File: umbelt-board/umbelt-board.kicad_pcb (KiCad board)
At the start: 4 copper layers, 56.6 x 20.3 mm, 101 parts, among them J1 USB4105-GF-A, J2 Conn_01x06, J3 SM04B-SRSS-TB, J4 TC2050-IDC-NL, J5 BM02B-ACHLKS, J6 Conn_Flex_Motor, J7 Conn_Indiv_Motor, Q1 AO3415A, SW1 KMR231NG-ULC-LFS, SW2 CUS-12TB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

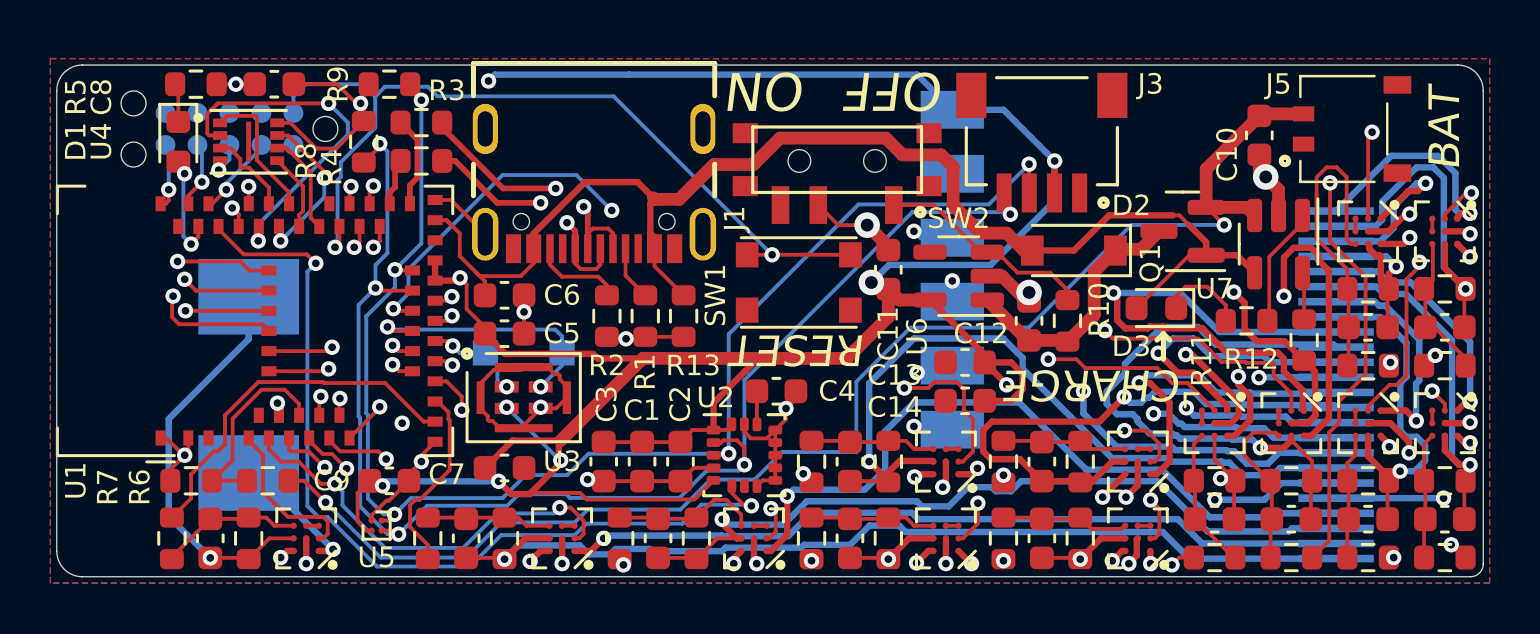
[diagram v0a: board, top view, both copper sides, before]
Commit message: complete routing. passes important DRC checks
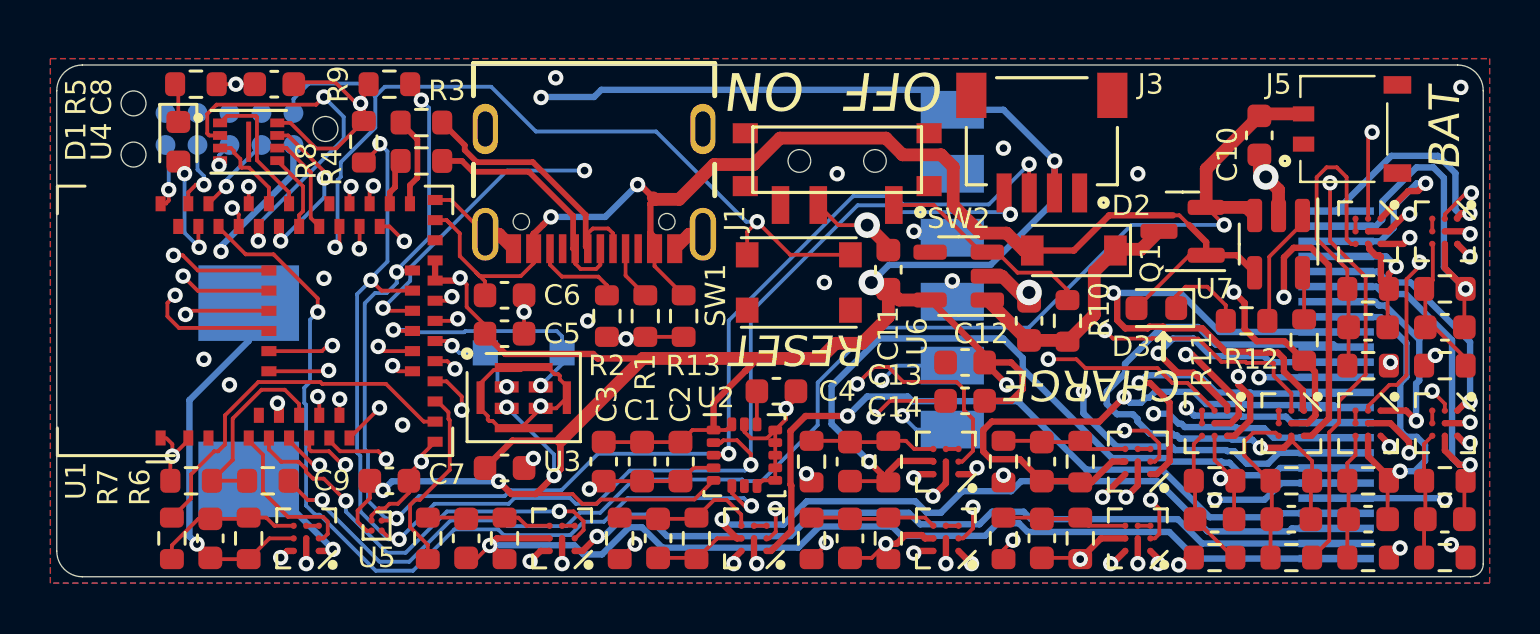
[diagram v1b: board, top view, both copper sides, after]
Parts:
- moved J7 0.25 mm to (134.6, 119.6)
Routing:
- net +3V3: track 239.8 -> 259.8 mm, vias 23 -> 25
- net GND: track 77.8 -> 84.3 mm, vias 26 -> 37
- net /SCL: track 55.0 -> 57.7 mm
- net /motor_drivers/OUT+_1: track 38.2 -> 40.3 mm
- net /motor_drivers/OUT+_4: track 30.3 -> 32.3 mm
- net /MOTOR_PWM_10: track 56.9 -> 58.7 mm
- net /MOTOR_PWM_3: track 31.1 -> 32.5 mm
- net /MOTOR_PWM_2: track 20.3 -> 21.7 mm
- net /SDA: track 55.7 -> 57.0 mm
- net /MOTOR_PWM_7: track 58.4 -> 59.6 mm
- net /MOTOR_PWM_5: track 37.8 -> 38.9 mm
- net /motor_drivers/OUT-_1: track 31.4 -> 32.5 mm
- net /MOTOR_EN_6: track 48.4 -> 49.5 mm
- net /A0: track 35.7 -> 36.7 mm
- net /motor_drivers/OUT-_2: track 28.8 -> 29.6 mm
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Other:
- board text added: "License: CERN-OHL-W v2+ github.com/cygann/umbelt-hw"

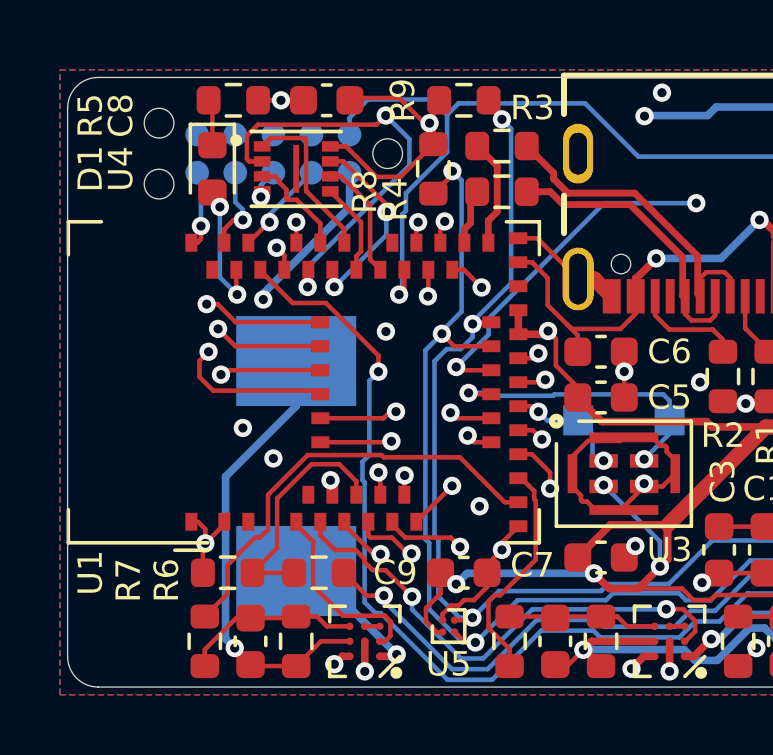
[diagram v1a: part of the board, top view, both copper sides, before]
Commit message: tweak ground pours
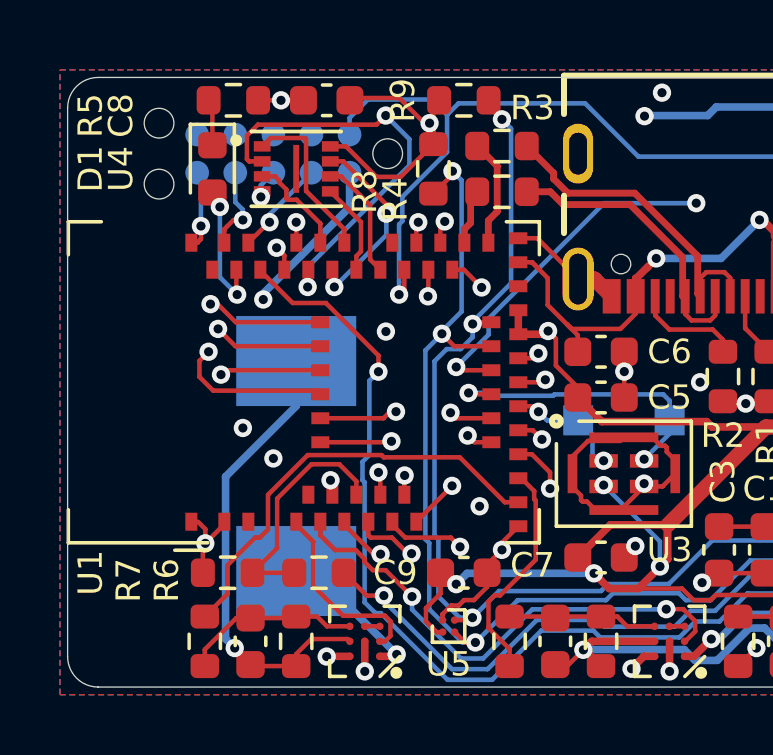
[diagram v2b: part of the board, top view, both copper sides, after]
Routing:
- net /D0: track 34.2 -> 32.0 mm
- net /MOTOR_EN_6: track 49.5 -> 48.9 mm

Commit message: complete flex pcb, generate gerbers for both boards
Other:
- rule pad_to_mask_clearance: 0.0508 -> 0

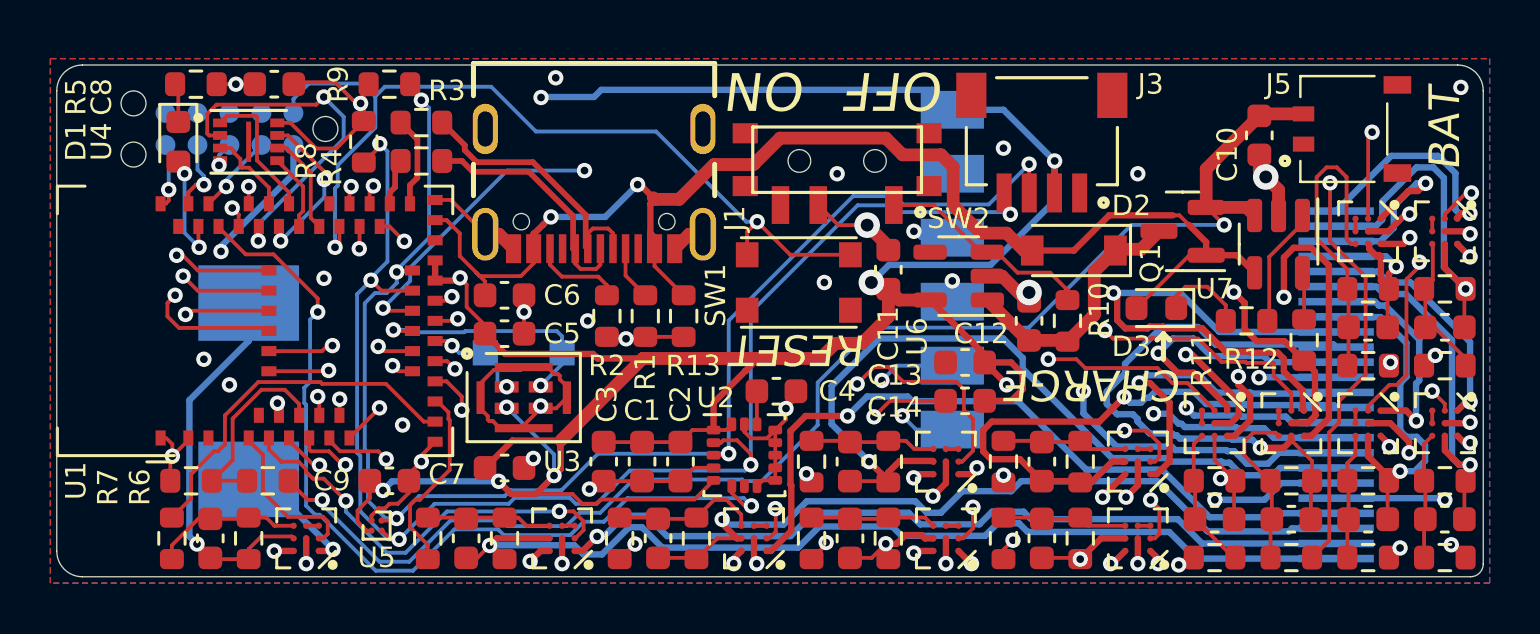
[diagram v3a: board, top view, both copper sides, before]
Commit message: fix SCL/SDA swap on magnetometer, generate outputs
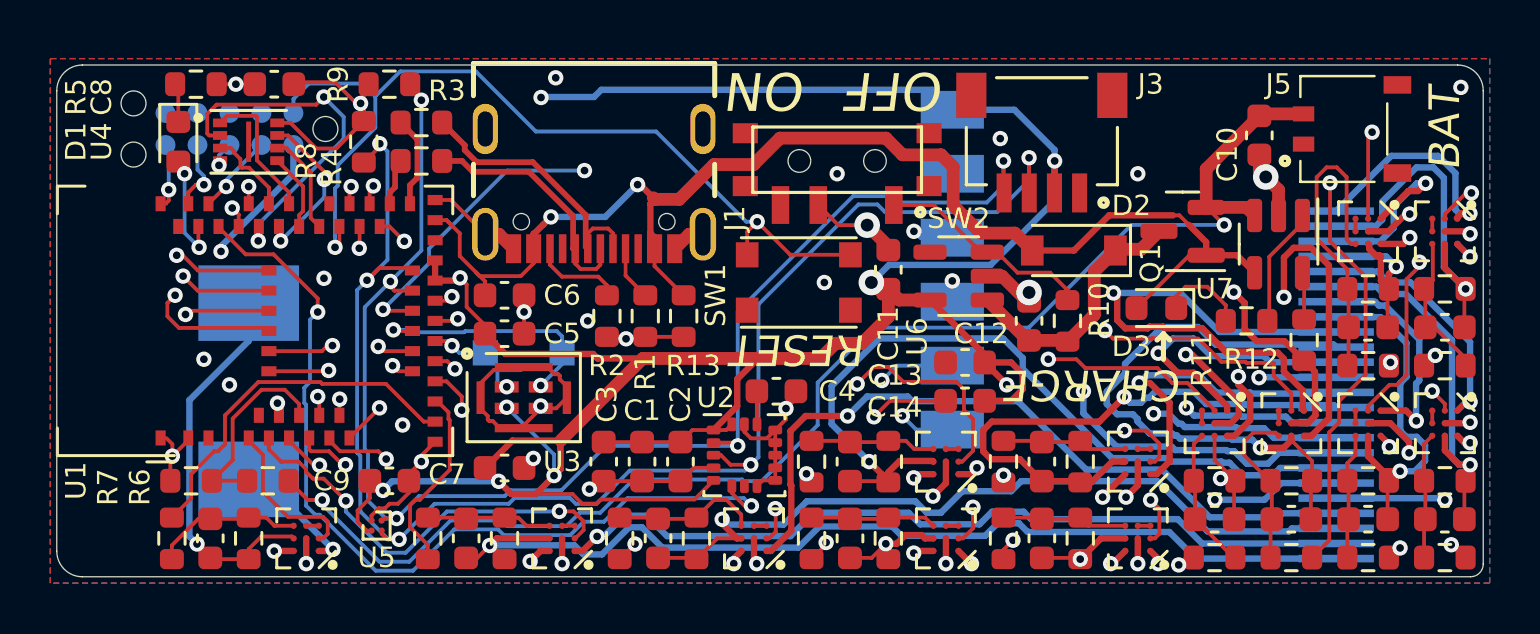
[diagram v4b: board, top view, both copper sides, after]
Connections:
- R8 pad 2: /SCL -> /SDA
- R9 pad 2: /SDA -> /SCL
- U5 pad A2: /SDA -> /SCL
- U5 pad B2: /SCL -> /SDA
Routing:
- net /SDA: track 57.0 -> 60.1 mm
- net /SCL: track 57.7 -> 57.1 mm
- net /RESET: track 35.1 -> 35.6 mm
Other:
- board text added: "V1.0.1"
- board text removed: "V1.0"
